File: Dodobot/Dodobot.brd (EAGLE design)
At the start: 98.8 x 80 mm, 43 parts, among them Q1 2N3904, Q2 2N3904, Q3 2N7000, Q4 2N7000

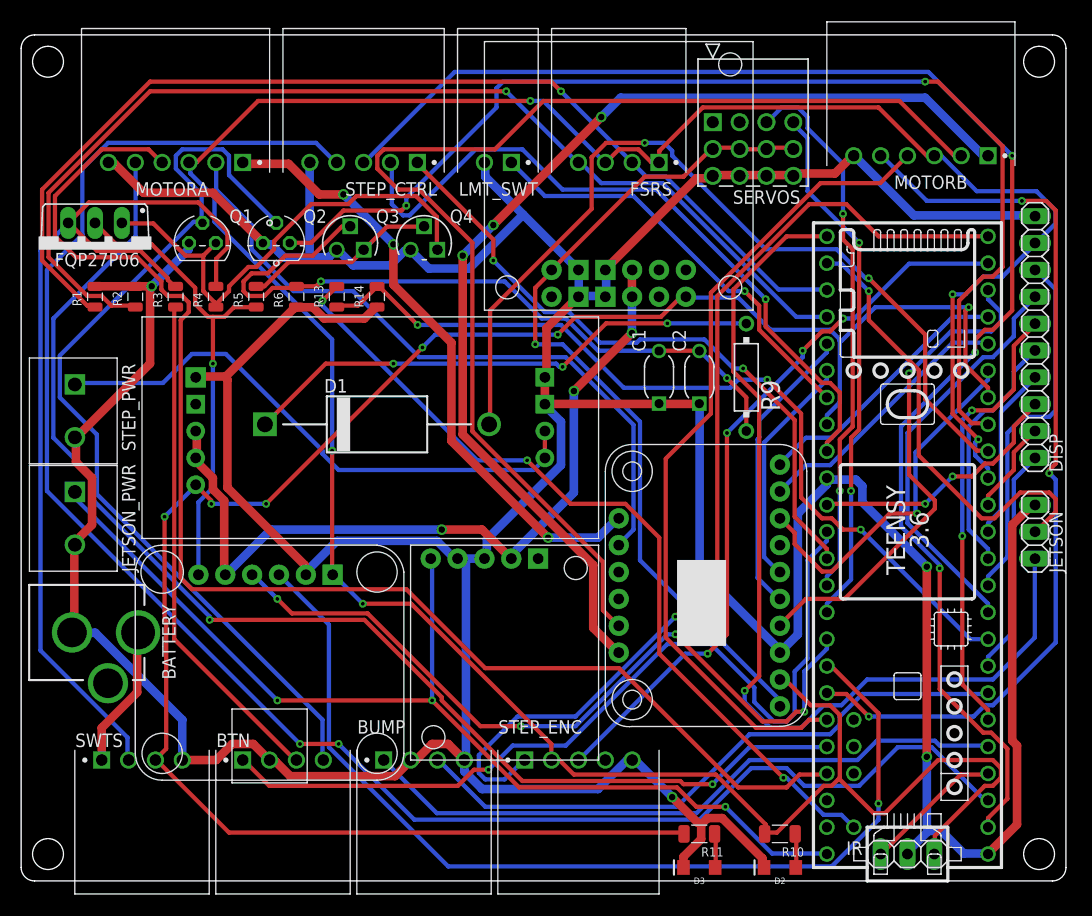
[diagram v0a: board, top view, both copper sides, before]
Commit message: fixing top connector positioning
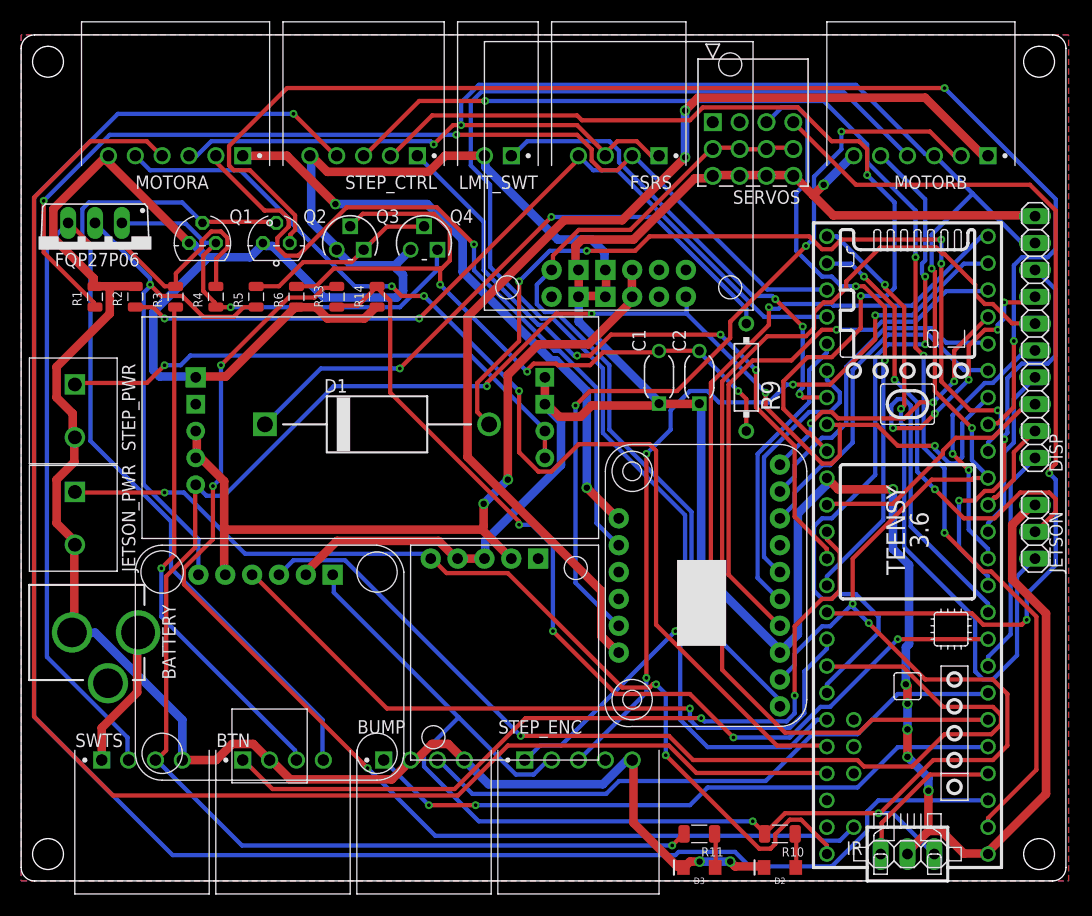
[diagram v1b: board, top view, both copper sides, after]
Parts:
- moved FSRS 0.64 mm to (60.3, 68.6)
- moved LMT_SWT 0.64 mm to (46.4, 68.6)
- moved MOTORA 0.64 mm to (21.0, 68.6)
- moved STEP_CTRL 0.64 mm to (37.5, 68.6)
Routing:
- net DIS_CARD_CS: track 42.5 -> 95.0 mm, vias 2 -> 0
- net MB_ENCA: track 77.4 -> 127.9 mm
- net MB2: track 114.6 -> 76.0 mm, vias 0 -> 3
- net SERVO1: track 50.2 -> 88.3 mm
- net N$14: track 79.5 -> 110.1 mm
- net RX_JETSON: track 91.0 -> 62.8 mm, vias 1 -> 2
- net FSR_SNS_2: track 102.7 -> 78.8 mm, vias 1 -> 2
- net VCC: track 277.1 -> 300.7 mm, vias 5 -> 8
- net TIC_RST: track 66.5 -> 87.5 mm, vias 1 -> 2
- net GND: track 517.4 -> 538.1 mm, vias 4 -> 9
- net MB_ENCB: track 85.6 -> 66.9 mm, vias 3 -> 2
- net MA_ENCA: track 128.3 -> 145.1 mm
- net TIC_TX: track 141.8 -> 125.0 mm, vias 3 -> 4
- net TIC_RX: track 165.9 -> 182.6 mm, vias 2 -> 1
- net STEP_ENCB: track 93.5 -> 77.3 mm, vias 1 -> 2
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- added copper zone on layer 1, net GND
- added copper zone on layer 16, net GND

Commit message: minor fixes. Correcting errors in library files
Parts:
- 12V_REG: value S18V20FX -> ELEC-169
- 5V_REG: value D24V50F5 -> ELEC-154
- 6V_REG: value D36V50FX -> ELEC-153
- BATTERY_MONITOR: value INA219 -> ELEC-133
- C1, C2: value FK24X5R0J226M -> 22uF
- MOTOR_DRIVER: value ADAFRUIT_TB6612 -> ELEC-134
- R1, R14, R2, R3, R4, R5: value CRCW08050000Z0EA -> 10K
- R10, R11: value WSLP1206R0500FEA -> 20
- R13: value CRCW08050000Z0EA -> 6K
- R6: value CRCW08050000Z0EA -> 100K
- R9: value (none) -> 10
- renumbered U$3 to MOTOR_DRIVER, U$4 to BATTERY_MONITOR, U$5 to 5V_REG, U$6 to 12V_REG, U$7 to 6V_REG
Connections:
- net GND: now also 12V_REG.GND_IN2
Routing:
- net GND: track 538.1 -> 540.6 mm
